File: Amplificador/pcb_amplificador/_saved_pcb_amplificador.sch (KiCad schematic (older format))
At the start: 139 parts, among them CON1 SJ-3523-SMT-TR, J1 Screw_Terminal_01x02, J2 Screw_Terminal_01x02, J3 Screw_Terminal_01x02, J4 Screw_Terminal_01x02, J5 Conn_01x03_Male, J6 Screw_Terminal_01x02, J7 Screw_Terminal_01x02, K1 FINDER-40.11-2016, M1 FDS9934C, M2 FDS9934C, Q1 BC860, Q10 BD139, Q11 BD140, Q12 BD139, Q13 2SA1943-O_Q_, Q14 2SC5200-O_Q, Q15 2SA1943-O_Q_, Q16 2SC5200-O_Q, Q17 2SAR514P5, Q18 BC860, Q19 BC860, Q2 BC860, Q20 2SAR514P5, Q21 2SCR514P5, Q22 2SCR514P5, Q23 2SCR514P5, Q24 2SAR514P5, Q25 2SCR514P5, Q26 BC817, Q27 BC817, Q28 BC807, Q29 BS170, Q3 BC850, Q4 BC850, Q5 BC860, Q6 BC860, Q7 BC850, Q8 2SCR514P5, Q9 2SCR514P5

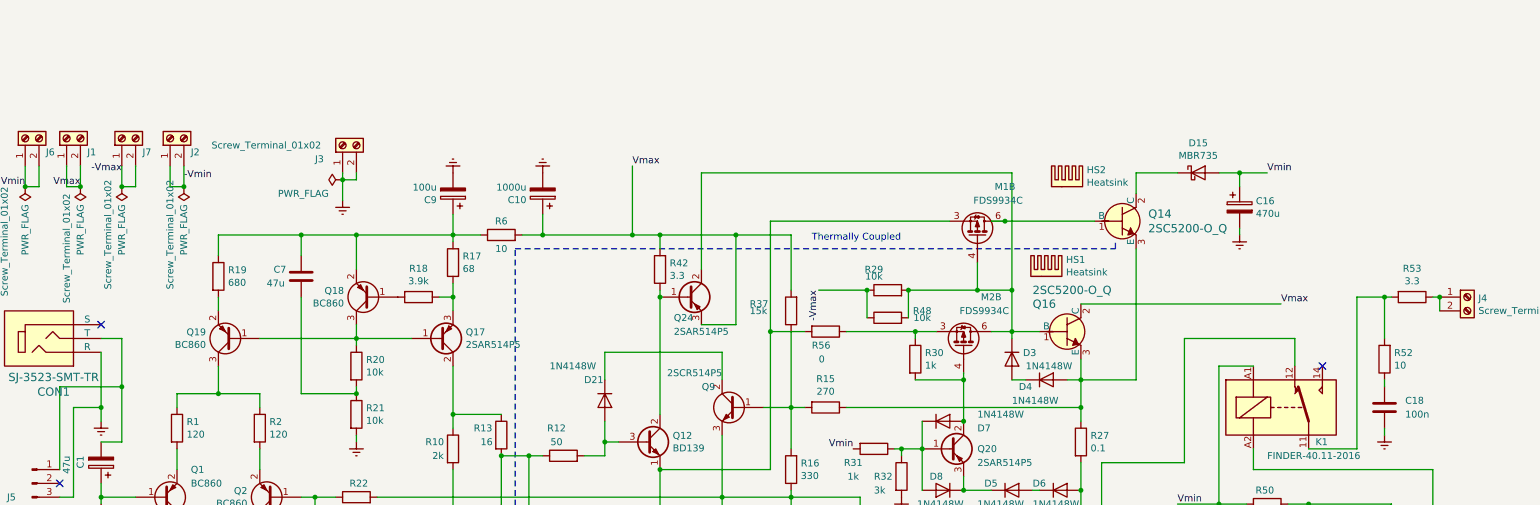
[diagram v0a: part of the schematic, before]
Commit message: Actualización de las especificaciones del amplificador
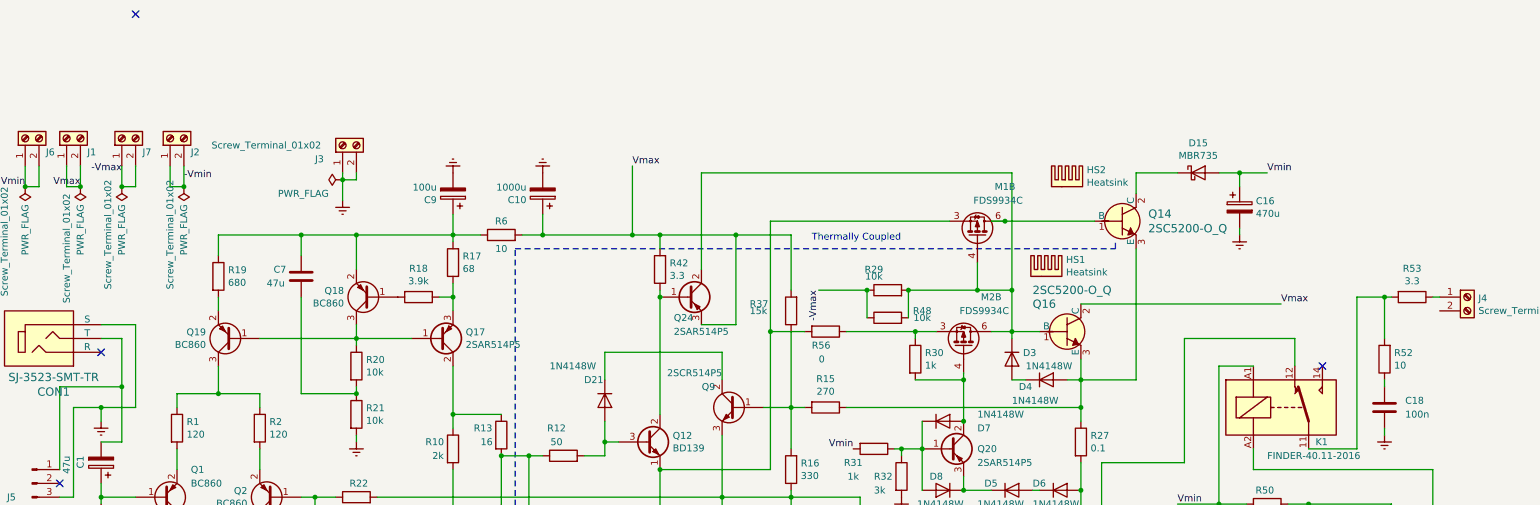
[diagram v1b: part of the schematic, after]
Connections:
- net Earth: now also CON1.1 (S); no longer CON1.3 (R)
- net at J4.1 (Pin_1), R53.1: no longer J4.2 (Pin_2)
- no-connect marks 3 -> 4
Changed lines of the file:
@@
 	1400 2000 1400 2350
-Wire Wire Line
-	1250 2100 1250 2500
 Wire Wire Line
 	950  2950 950  2350
@@
 Wire Wire Line
 	1050 2500 1250 2500
-Connection ~ 1250 2500
 Wire Wire Line
 	1250 2500 1250 2600
@@
 	0    -1   1    0
 $EndComp
-NoConn ~ 1250 1900
 Wire Wire Line
 	1100 750  1100 900
@@
 Wire Wire Line
 	10550 1700 10350 1700
-Connection ~ 10950 1700
-Wire Wire Line
-	10950 1800 10950 1700
 Wire Wire Line
 	6950 5450 7400 5450
@@
 	0    1    1    0
 $EndComp
+Wire Wire Line
+	1250 1900 1500 1900
+Wire Wire Line
+	1500 1900 1500 2500
+Wire Wire Line
+	1500 2500 1250 2500
+Connection ~ 1250 2500
+NoConn ~ 1250 2100
+NoConn ~ 1500 -350
 $EndSCHEMATC
